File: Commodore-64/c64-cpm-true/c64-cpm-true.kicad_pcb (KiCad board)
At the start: 2 copper layers, 105 x 130 mm, 51 parts, among them Q1 2N3906, U1 74S74, U10 74LS283, U11 74LS245, U12 4K7, U13 Z80CPU, U14 74LS245, U15 4K7, U2 74S04, U3 74LS367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

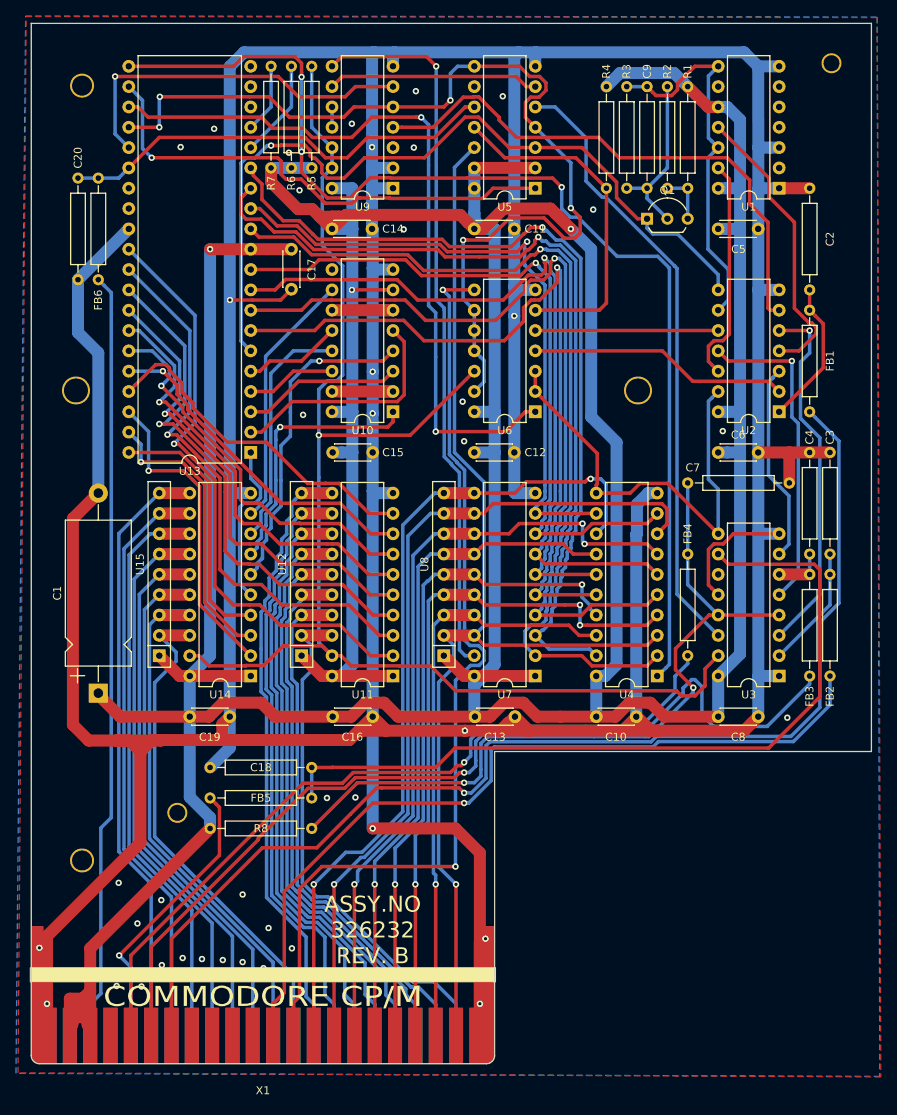
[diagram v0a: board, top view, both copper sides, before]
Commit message: Update to fit original CP/M case better
* Moved the left screwhole 0.5mm
* Moved the right screwhole 1mm
* Moved the top-right pinhole 0.2mm
* Removed the ground traces that went between card edge pads.
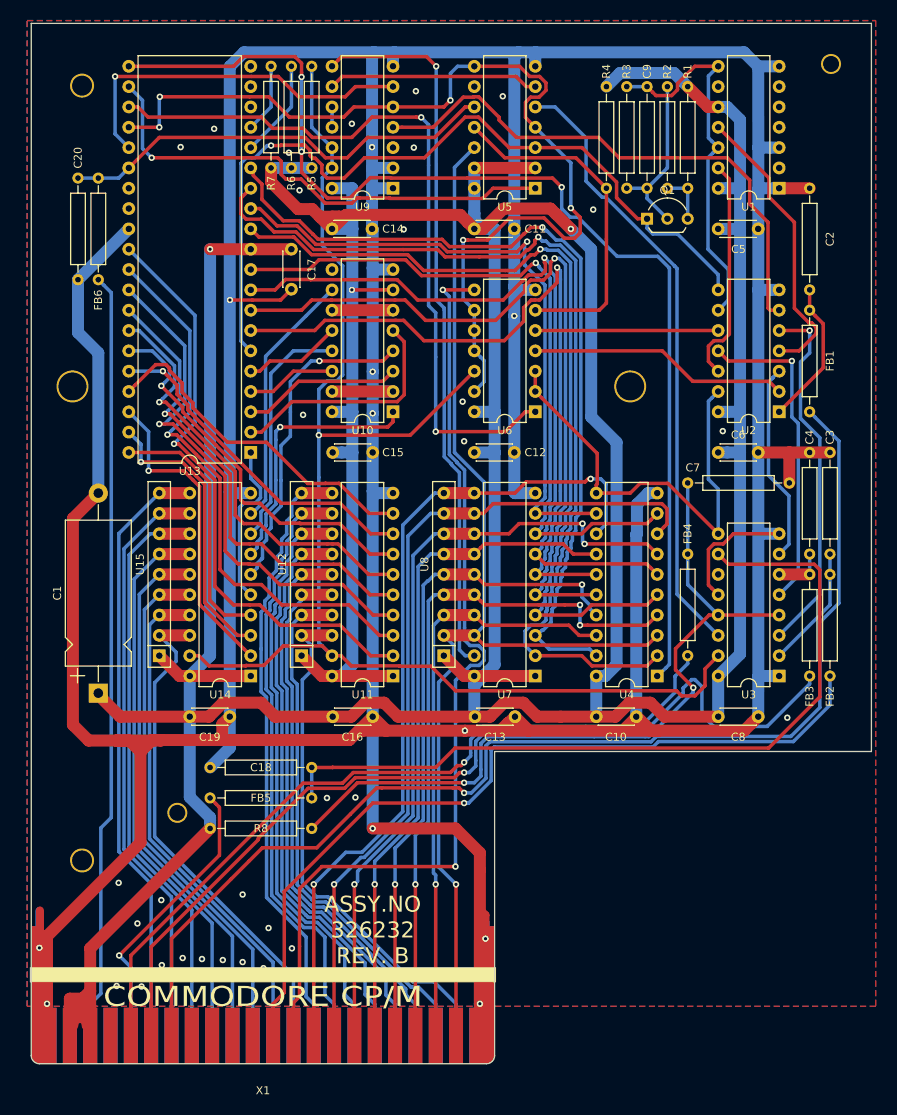
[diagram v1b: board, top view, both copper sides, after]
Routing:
- net GND: track 871.2 -> 891.4 mm
